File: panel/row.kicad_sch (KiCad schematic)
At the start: 16 parts

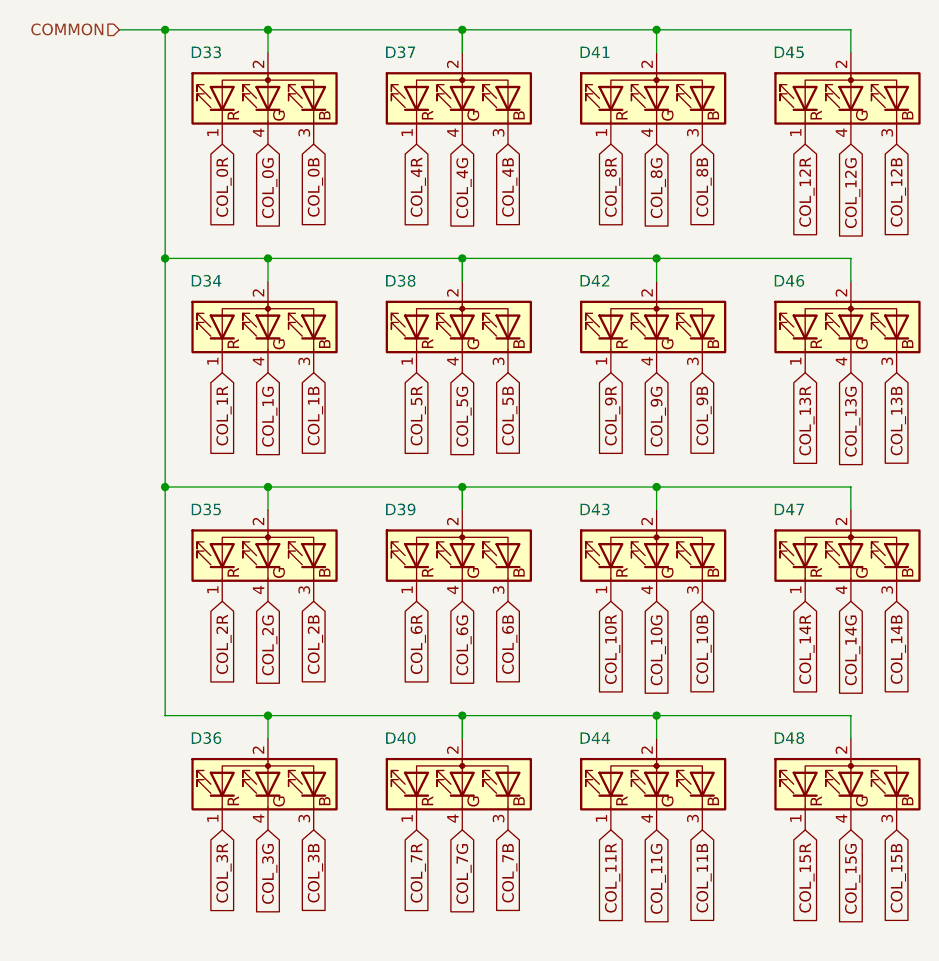
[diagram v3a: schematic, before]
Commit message: Routed all data signals
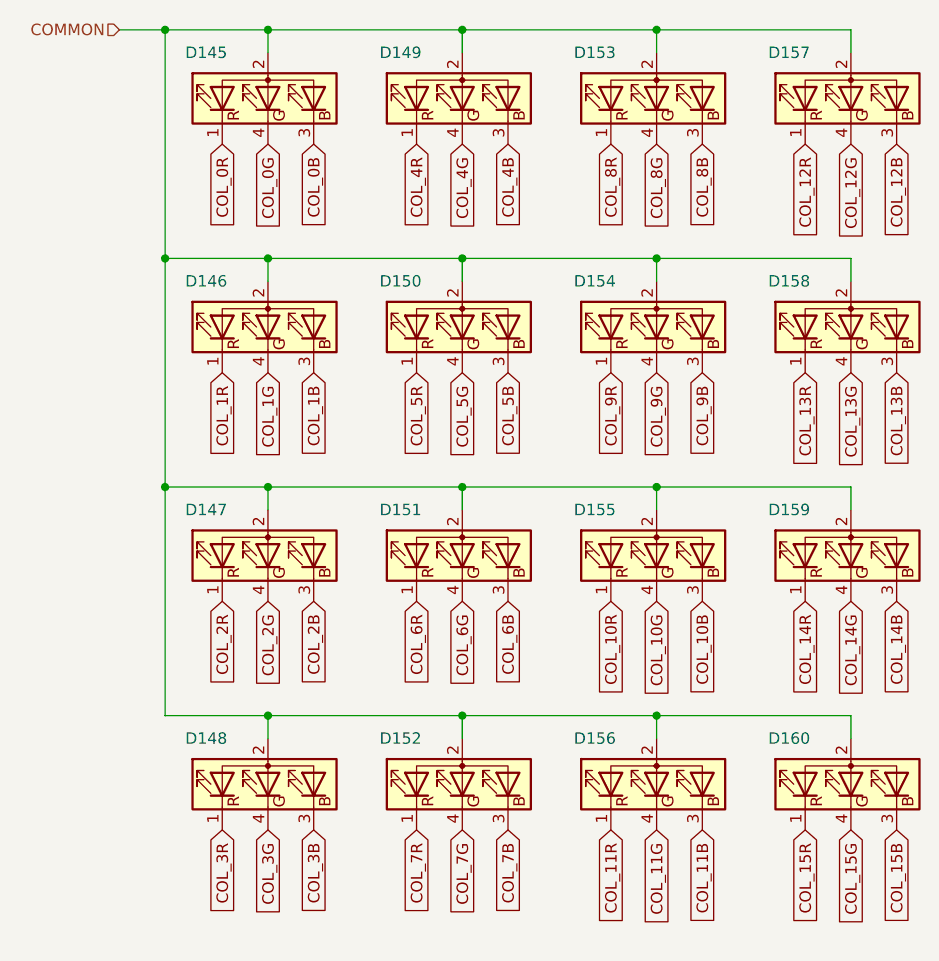
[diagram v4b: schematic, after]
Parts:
- renumbered D33 to D145, D34 to D146, D35 to D147, D36 to D148, D37 to D149, D38 to D150, D39 to D151, D40 to D152, D41 to D153, D42 to D154, D43 to D155, D44 to D156, D45 to D157, D46 to D158, D47 to D159, D48 to D160
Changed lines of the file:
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@@
   (symbol (lib_id "Device:LED_RABG") (at 113.03 58.42 90)
     (in_bom yes) (on_board yes)
-    (property "Reference" "D33" (id 0) (at 106.172 53.34 90))
+    (property "Reference" "D145" (id 0) (at 106.172 53.34 90))
     (property "Value" "LED_RABG" (id 1) (at 121.92 58.42 0)
       (effects (font (size 1.27 1.27)) hide)
@@
   (symbol (lib_id "Device:LED_RABG") (at 113.03 83.82 90)
     (in_bom yes) (on_board yes)
-    (property "Reference" "D34" (id 0) (at 106.172 78.74 90))
+    (property "Reference" "D146" (id 0) (at 106.172 78.74 90))
     (property "Value" "LED_RABG" (id 1) (at 121.92 83.82 0)
       (effects (font (size 1.27 1.27)) hide)
@@
   (symbol (lib_id "Device:LED_RABG") (at 113.03 109.22 90)
     (in_bom yes) (on_board yes)
-    (property "Reference" "D35" (id 0) (at 106.172 104.14 90))
+    (property "Reference" "D147" (id 0) (at 106.172 104.14 90))
     (property "Value" "LED_RABG" (id 1) (at 121.92 109.22 0)
       (effects (font (size 1.27 1.27)) hide)
@@
   (symbol (lib_id "Device:LED_RABG") (at 113.03 134.62 90)
     (in_bom yes) (on_board yes)
-    (property "Reference" "D36" (id 0) (at 106.172 129.54 90))
+    (property "Reference" "D148" (id 0) (at 106.172 129.54 90))
     (property "Value" "LED_RABG" (id 1) (at 121.92 134.62 0)
       (effects (font (size 1.27 1.27)) hide)
@@
   (symbol (lib_id "Device:LED_RABG") (at 134.62 58.42 90)
     (in_bom yes) (on_board yes)
-    (property "Reference" "D37" (id 0) (at 127.762 53.34 90))
+    (property "Reference" "D149" (id 0) (at 127.762 53.34 90))
     (property "Value" "LED_RABG" (id 1) (at 143.51 58.42 0)
       (effects (font (size 1.27 1.27)) hide)
@@
   (symbol (lib_id "Device:LED_RABG") (at 134.62 83.82 90)
     (in_bom yes) (on_board yes)
-    (property "Reference" "D38" (id 0) (at 127.762 78.74 90))
+    (property "Reference" "D150" (id 0) (at 127.762 78.74 90))
     (property "Value" "LED_RABG" (id 1) (at 143.51 83.82 0)
       (effects (font (size 1.27 1.27)) hide)
@@
   (symbol (lib_id "Device:LED_RABG") (at 134.62 109.22 90)
     (in_bom yes) (on_board yes)
-    (property "Reference" "D39" (id 0) (at 127.762 104.14 90))
+    (property "Reference" "D151" (id 0) (at 127.762 104.14 90))
     (property "Value" "LED_RABG" (id 1) (at 143.51 109.22 0)
       (effects (font (size 1.27 1.27)) hide)
@@
   (symbol (lib_id "Device:LED_RABG") (at 134.62 134.62 90)
     (in_bom yes) (on_board yes)
-    (property "Reference" "D40" (id 0) (at 127.762 129.54 90))
+    (property "Reference" "D152" (id 0) (at 127.762 129.54 90))
     (property "Value" "LED_RABG" (id 1) (at 143.51 134.62 0)
       (effects (font (size 1.27 1.27)) hide)
@@
   (symbol (lib_id "Device:LED_RABG") (at 156.21 58.42 90)
     (in_bom yes) (on_board yes)
-    (property "Reference" "D41" (id 0) (at 149.352 53.34 90))
+    (property "Reference" "D153" (id 0) (at 149.352 53.34 90))
     (property "Value" "LED_RABG" (id 1) (at 165.1 58.42 0)
       (effects (font (size 1.27 1.27)) hide)
@@
   (symbol (lib_id "Device:LED_RABG") (at 156.21 83.82 90)
     (in_bom yes) (on_board yes)
-    (property "Reference" "D42" (id 0) (at 149.352 78.74 90))
+    (property "Reference" "D154" (id 0) (at 149.352 78.74 90))
     (property "Value" "LED_RABG" (id 1) (at 165.1 83.82 0)
       (effects (font (size 1.27 1.27)) hide)
@@
   (symbol (lib_id "Device:LED_RABG") (at 156.21 109.22 90)
     (in_bom yes) (on_board yes)
-    (property "Reference" "D43" (id 0) (at 149.352 104.14 90))
+    (property "Reference" "D155" (id 0) (at 149.352 104.14 90))
     (property "Value" "LED_RABG" (id 1) (at 165.1 109.22 0)
       (effects (font (size 1.27 1.27)) hide)
@@
   (symbol (lib_id "Device:LED_RABG") (at 156.21 134.62 90)
     (in_bom yes) (on_board yes)
-    (property "Reference" "D44" (id 0) (at 149.352 129.54 90))
+    (property "Reference" "D156" (id 0) (at 149.352 129.54 90))
     (property "Value" "LED_RABG" (id 1) (at 165.1 134.62 0)
       (effects (font (size 1.27 1.27)) hide)
@@
   (symbol (lib_id "Device:LED_RABG") (at 177.8 58.42 90)
     (in_bom yes) (on_board yes)
-    (property "Reference" "D45" (id 0) (at 170.942 53.34 90))
+    (property "Reference" "D157" (id 0) (at 170.942 53.34 90))
     (property "Value" "LED_RABG" (id 1) (at 186.69 58.42 0)
       (effects (font (size 1.27 1.27)) hide)
@@
   (symbol (lib_id "Device:LED_RABG") (at 177.8 83.82 90)
     (in_bom yes) (on_board yes)
-    (property "Reference" "D46" (id 0) (at 170.942 78.74 90))
+    (property "Reference" "D158" (id 0) (at 170.942 78.74 90))
     (property "Value" "LED_RABG" (id 1) (at 186.69 83.82 0)
       (effects (font (size 1.27 1.27)) hide)
@@
   (symbol (lib_id "Device:LED_RABG") (at 177.8 109.22 90)
     (in_bom yes) (on_board yes)
-    (property "Reference" "D47" (id 0) (at 170.942 104.14 90))
+    (property "Reference" "D159" (id 0) (at 170.942 104.14 90))
     (property "Value" "LED_RABG" (id 1) (at 186.69 109.22 0)
       (effects (font (size 1.27 1.27)) hide)
@@
   (symbol (lib_id "Device:LED_RABG") (at 177.8 134.62 90)
     (in_bom yes) (on_board yes)
-    (property "Reference" "D48" (id 0) (at 170.942 129.54 90))
+    (property "Reference" "D160" (id 0) (at 170.942 129.54 90))
     (property "Value" "LED_RABG" (id 1) (at 186.69 134.62 0)
       (effects (font (size 1.27 1.27)) hide)
